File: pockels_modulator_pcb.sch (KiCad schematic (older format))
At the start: 11 parts, among them J1 Conn_Coaxial

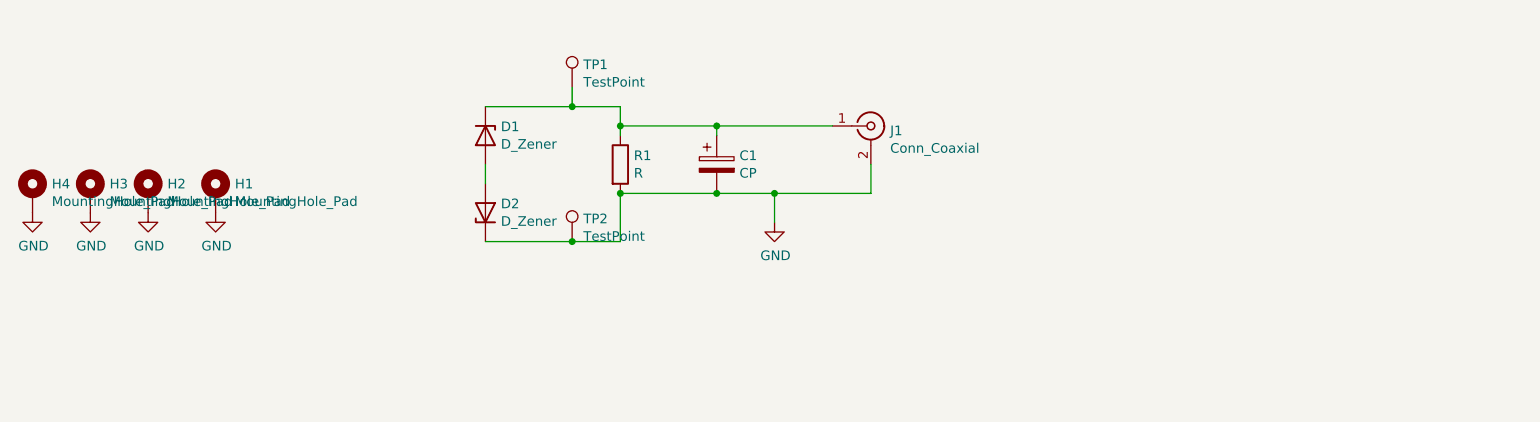
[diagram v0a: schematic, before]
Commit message: revised pockels modulator PCB to include thermal vias, chip for thermal sensing, SMD connector
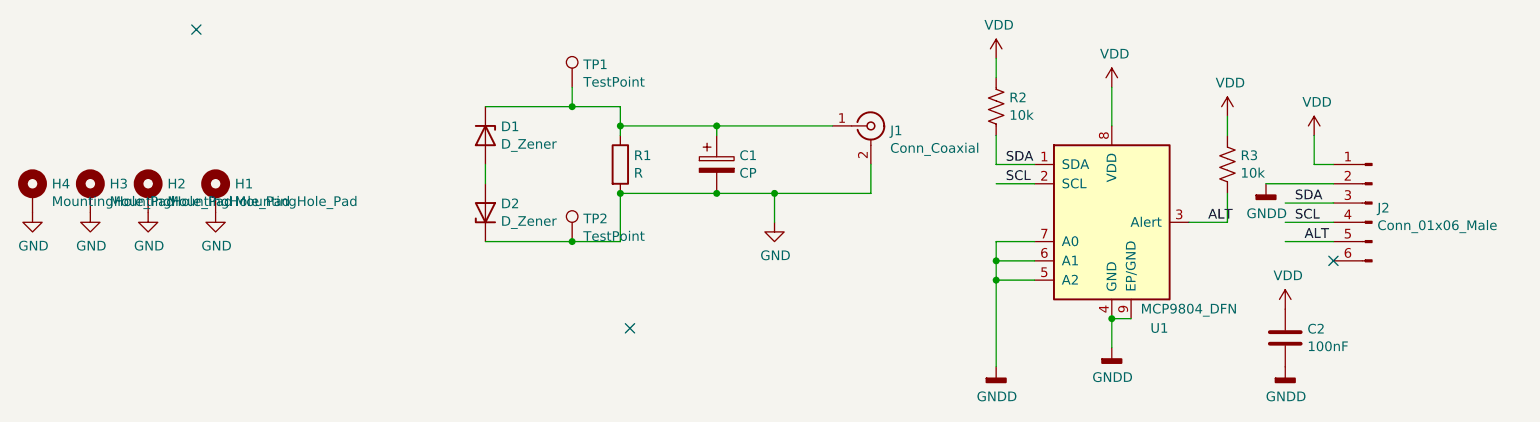
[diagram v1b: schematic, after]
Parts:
- added C2: 100nF, Capacitor_SMD:C_0805_2012Metric_Pad1.15x1.40mm_HandSolder, symbol Device:C
- added J2: Conn_01x06_Male, my_library_foot:S6B-XH-SM4-TB, symbol Connector:Conn_01x06_Male
- added R2, R3: 10k, Resistor_SMD:R_0805_2012Metric_Pad1.15x1.40mm_HandSolder, symbol Device:R_US
- added U1: MCP9804_DFN, Package_DFN_QFN:DFN-8-1EP_3x2mm_P0.5mm_EP1.3x1.5mm_HandSolder, symbol Sensor_Temperature:MCP9804_DFN
- C1: footprint my_library_foot:pockels_chip_10mm -> my_library_foot:pockels_chip_10mm_thermal
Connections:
- net labels added: ALT, GNDD, SCL, SDA, VDD
- wire segments 17 -> 39
- no-connect marks 0 -> 3
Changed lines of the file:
@@
 F 0 "C1" H 4968 3246 50  0000 L CNN
 F 1 "CP" H 4968 3155 50  0000 L CNN
-F 2 "my_library_foot:pockels_chip_10mm" H 4888 3050 50  0001 C CNN
+F 2 "my_library_foot:pockels_chip_10mm_thermal" H 4888 3050 50  0001 C CNN
 F 3 "~" H 4850 3200 50  0001 C CNN
 	1    4850 3200
@@
 	1    0    0    -1
 $EndComp
+$Comp
+L Sensor_Temperature:MCP9804_DFN U1
+U 1 1 5FF4B793
+P 6900 3500
+F 0 "U1" H 7100 2950 50  0000 L CNN
+F 1 "MCP9804_DFN" H 7050 3050 50  0000 L CNN
+F 2 "Package_DFN_QFN:DFN-8-1EP_3x2mm_P0.5mm_EP1.3x1.5mm_HandSolder" H 5800 3000 50  0001 C CNN
+F 3 "http://ww1.microchip.com/downloads/en/DeviceDoc/22203b.pdf" H 6650 3950 50  0001 C CNN
+	1    6900 3500
+	1    0    0    -1
+$EndComp
+$Comp
+L power:VDD #PWR04
+U 1 1 5FF4CD79
+P 6900 2800
+F 0 "#PWR04" H 6900 2650 50  0001 C CNN
+F 1 "VDD" H 6915 2973 50  0000 C CNN
+F 2 "" H 6900 2800 50  0001 C CNN
+F 3 "" H 6900 2800 50  0001 C CNN
+	1    6900 2800
+	1    0    0    -1
+$EndComp
+Wire Wire Line
+	6900 2800 6900 3000
+Wire Wire Line
+	8050 3200 7950 3200
+Wire Wire Line
+	7950 3200 7950 3050
+$Comp
+L power:VDD #PWR010
+U 1 1 5FF4FF71
+P 7950 3050
+F 0 "#PWR010" H 7950 2900 50  0001 C CNN
+F 1 "VDD" H 7965 3223 50  0000 C CNN
+F 2 "" H 7950 3050 50  0001 C CNN
+F 3 "" H 7950 3050 50  0001 C CNN
+	1    7950 3050
+	1    0    0    -1
+$EndComp
+Wire Wire Line
+	7700 3300 8050 3300
+Wire Wire Line
+	7800 3400 8050 3400
+Wire Wire Line
+	7800 3500 8050 3500
+Text Label 7850 3400 0    50   ~ 0
+SDA
+Text Label 7850 3500 0    50   ~ 0
+SCL
+Wire Wire Line
+	6500 3200 6300 3200
+Wire Wire Line
+	6500 3300 6300 3300
+Text Label 6350 3200 0    50   ~ 0
+SDA
+Text Label 6350 3300 0    50   ~ 0
+SCL
+Wire Wire Line
+	6500 3800 6300 3800
+Wire Wire Line
+	6500 3700 6300 3700
+Wire Wire Line
+	6300 3700 6300 3800
+Connection ~ 6300 3800
+Wire Wire Line
+	6500 3600 6300 3600
+Wire Wire Line
+	6300 3600 6300 3700
+Connection ~ 6300 3700
+Wire Wire Line
+	7000 4000 6900 4000
+Wire Wire Line
+	6900 4000 6900 4150
+Connection ~ 6900 4000
+Wire Wire Line
+	8050 3600 7800 3600
+Text Label 7900 3600 0    50   ~ 0
+ALT
+Wire Wire Line
+	7300 3500 7500 3500
+Text Label 7400 3500 0    50   ~ 0
+ALT
+$Comp
+L Device:C C2
+U 1 1 5FF59802
+P 7800 4100
+F 0 "C2" H 7915 4146 50  0000 L CNN
+F 1 "100nF" H 7915 4055 50  0000 L CNN
+F 2 "Capacitor_SMD:C_0805_2012Metric_Pad1.15x1.40mm_HandSolder" H 7838 3950 50  0001 C CNN
+F 3 "~" H 7800 4100 50  0001 C CNN
+	1    7800 4100
+	1    0    0    -1
+$EndComp
+$Comp
+L power:VDD #PWR08
+U 1 1 5FF5A155
+P 7800 3950
+F 0 "#PWR08" H 7800 3800 50  0001 C CNN
+F 1 "VDD" H 7815 4123 50  0000 C CNN
+F 2 "" H 7800 3950 50  0001 C CNN
+F 3 "" H 7800 3950 50  0001 C CNN
+	1    7800 3950
+	1    0    0    -1
+$EndComp
+$Comp
+L Device:R_US R3
+U 1 1 5FF5AD39
+P 7500 3200
+F 0 "R3" H 7568 3246 50  0000 L CNN
+F 1 "10k" H 7568 3155 50  0000 L CNN
+F 2 "Resistor_SMD:R_0805_2012Metric_Pad1.15x1.40mm_HandSolder" V 7540 3190 50  0001 C CNN
+F 3 "~" H 7500 3200 50  0001 C CNN
+	1    7500 3200
+	1    0    0    -1
+$EndComp
+Wire Wire Line
+	7500 3350 7500 3500
+$Comp
+L power:VDD #PWR06
+U 1 1 5FF5E3D3
+P 7500 2950
+F 0 "#PWR06" H 7500 2800 50  0001 C CNN
+F 1 "VDD" H 7515 3123 50  0000 C CNN
+F 2 "" H 7500 2950 50  0001 C CNN
+F 3 "" H 7500 2950 50  0001 C CNN
+	1    7500 2950
+	1    0    0    -1
+$EndComp
+Wire Wire Line
+	7500 2950 7500 3050
+$Comp
+L Device:R_US R2
+U 1 1 5FF5F423
+P 6300 2900
+F 0 "R2" H 6368 2946 50  0000 L CNN
+F 1 "10k" H 6368 2855 50  0000 L CNN
+F 2 "Resistor_SMD:R_0805_2012Metric_Pad1.15x1.40mm_HandSolder" V 6340 2890 50  0001 C CNN
+F 3 "~" H 6300 2900 50  0001 C CNN
+	1    6300 2900
+	1    0    0    -1
+$EndComp
+Wire Wire Line
+	6300 3050 6300 3200
+$Comp
+L power:VDD #PWR02
+U 1 1 5FF6033B
+P 6300 2650
+F 0 "#PWR02" H 6300 2500 50  0001 C CNN
+F 1 "VDD" H 6315 2823 50  0000 C CNN
+F 2 "" H 6300 2650 50  0001 C CNN
+F 3 "" H 6300 2650 50  0001 C CNN
+	1    6300 2650
+	1    0    0    -1
+$EndComp
+Wire Wire Line
+	6300 2650 6300 2750
+Wire Wire Line
+	6300 3800 6300 4250
+$Comp
+L power:GNDD #PWR0105
+U 1 1 5FF63E84
+P 6300 4250
+F 0 "#PWR0105" H 6300 4000 50  0001 C CNN
+F 1 "GNDD" H 6304 4095 50  0000 C CNN
+F 2 "" H 6300 4250 50  0001 C CNN
+F 3 "" H 6300 4250 50  0001 C CNN
+	1    6300 4250
+	1    0    0    -1
+$EndComp
+$Comp
+L power:GNDD #PWR0106
+U 1 1 5FF645C1
+P 6900 4150
+F 0 "#PWR0106" H 6900 3900 50  0001 C CNN
+F 1 "GNDD" H 6904 3995 50  0000 C CNN
+F 2 "" H 6900 4150 50  0001 C CNN
+F 3 "" H 6900 4150 50  0001 C CNN
+	1    6900 4150
+	1    0    0    -1
+$EndComp
+$Comp
+L power:GNDD #PWR0107
+U 1 1 5FF64A4E
+P 7800 4250
+F 0 "#PWR0107" H 7800 4000 50  0001 C CNN
+F 1 "GNDD" H 7804 4095 50  0000 C CNN
+F 2 "" H 7800 4250 50  0001 C CNN
+F 3 "" H 7800 4250 50  0001 C CNN
+	1    7800 4250
+	1    0    0    -1
+$EndComp
+$Comp
+L power:GNDD #PWR0108
+U 1 1 5FF65065
+P 7700 3300
+F 0 "#PWR0108" H 7700 3050 50  0001 C CNN
+F 1 "GNDD" H 7704 3145 50  0000 C CNN
+F 2 "" H 7700 3300 50  0001 C CNN
+F 3 "" H 7700 3300 50  0001 C CNN
+	1    7700 3300
+	1    0    0    -1
+$EndComp
+$Comp
+L Connector:Conn_01x06_Male J2
+U 1 1 5FF6D550
+P 8250 3400
+F 0 "J2" H 8222 3374 50  0000 R CNN
+F 1 "Conn_01x06_Male" H 8222 3283 50  0000 R CNN
+F 2 "my_library_foot:S6B-XH-SM4-TB" H 8250 3400 50  0001 C CNN
+F 3 "~" H 8250 3400 50  0001 C CNN
+	1    8250 3400
+	-1   0    0    -1
+$EndComp
+NoConn ~ 8050 3700
+NoConn ~ 4400 4050
+NoConn ~ 2150 2500
 $EndSCHEMATC

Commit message: updated for new 5mm chips to version 3
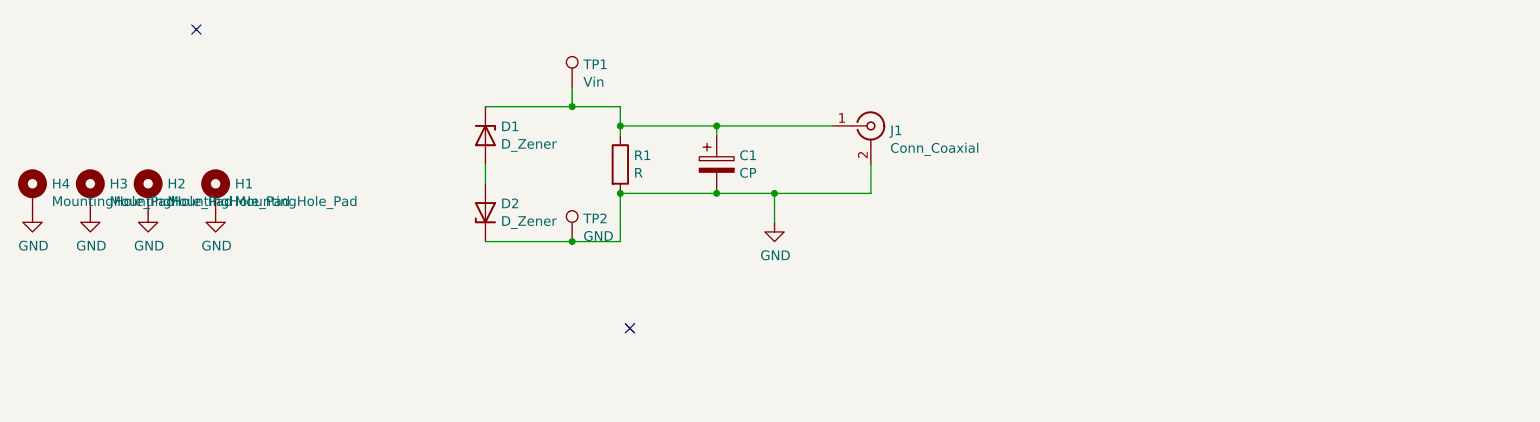
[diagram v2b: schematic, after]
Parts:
- removed C2: 100nF, Capacitor_SMD:C_0805_2012Metric_Pad1.15x1.40mm_HandSolder, symbol Device:C
- removed J2: Conn_01x06_Male, my_library_foot:S6B-XH-SM4-TB, symbol Connector:Conn_01x06_Male
- removed R2, R3: 10k, Resistor_SMD:R_0805_2012Metric_Pad1.15x1.40mm_HandSolder, symbol Device:R_US
- removed U1: MCP9804_DFN, Package_DFN_QFN:DFN-8-1EP_3x2mm_P0.5mm_EP1.3x1.5mm_HandSolder, symbol Sensor_Temperature:MCP9804_DFN
- TP1: value TestPoint -> Vin
- TP2: value TestPoint -> GND
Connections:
- net labels removed: ALT, GNDD, SCL, SDA, VDD
- wire segments 39 -> 17
- no-connect marks 3 -> 2
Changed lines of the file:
@@
 P 4100 2800
 F 0 "TP1" H 4158 2918 50  0000 L CNN
-F 1 "TestPoint" H 4158 2827 50  0000 L CNN
+F 1 "Vin" H 4158 2827 50  0000 L CNN
 F 2 "my_library_foot:TestPoint_Keystone_5000-5004_Miniature" H 4300 2800 50  0001 C CNN
 F 3 "~" H 4300 2800 50  0001 C CNN
@@
 P 4100 3600
 F 0 "TP2" H 4158 3718 50  0000 L CNN
-F 1 "TestPoint" H 4158 3627 50  0000 L CNN
+F 1 "GND" H 4158 3627 50  0000 L CNN
 F 2 "my_library_foot:TestPoint_Keystone_5000-5004_Miniature" H 4300 3600 50  0001 C CNN
 F 3 "~" H 4300 3600 50  0001 C CNN
@@
 	1    0    0    -1
 $EndComp
-$Comp
-L Sensor_Temperature:MCP9804_DFN U1
-U 1 1 5FF4B793
-P 6900 3500
-F 0 "U1" H 7100 2950 50  0000 L CNN
-F 1 "MCP9804_DFN" H 7050 3050 50  0000 L CNN
-F 2 "Package_DFN_QFN:DFN-8-1EP_3x2mm_P0.5mm_EP1.3x1.5mm_HandSolder" H 5800 3000 50  0001 C CNN
-F 3 "http://ww1.microchip.com/downloads/en/DeviceDoc/22203b.pdf" H 6650 3950 50  0001 C CNN
-	1    6900 3500
-	1    0    0    -1
-$EndComp
-$Comp
-L power:VDD #PWR04
-U 1 1 5FF4CD79
-P 6900 2800
-F 0 "#PWR04" H 6900 2650 50  0001 C CNN
-F 1 "VDD" H 6915 2973 50  0000 C CNN
-F 2 "" H 6900 2800 50  0001 C CNN
-F 3 "" H 6900 2800 50  0001 C CNN
-	1    6900 2800
-	1    0    0    -1
-$EndComp
-Wire Wire Line
-	6900 2800 6900 3000
-Wire Wire Line
-	8050 3200 7950 3200
-Wire Wire Line
-	7950 3200 7950 3050
-$Comp
-L power:VDD #PWR010
-U 1 1 5FF4FF71
-P 7950 3050
-F 0 "#PWR010" H 7950 2900 50  0001 C CNN
-F 1 "VDD" H 7965 3223 50  0000 C CNN
-F 2 "" H 7950 3050 50  0001 C CNN
-F 3 "" H 7950 3050 50  0001 C CNN
-	1    7950 3050
-	1    0    0    -1
-$EndComp
-Wire Wire Line
-	7700 3300 8050 3300
-Wire Wire Line
-	7800 3400 8050 3400
-Wire Wire Line
-	7800 3500 8050 3500
-Text Label 7850 3400 0    50   ~ 0
-SDA
-Text Label 7850 3500 0    50   ~ 0
-SCL
-Wire Wire Line
-	6500 3200 6300 3200
-Wire Wire Line
-	6500 3300 6300 3300
-Text Label 6350 3200 0    50   ~ 0
-SDA
-Text Label 6350 3300 0    50   ~ 0
-SCL
-Wire Wire Line
-	6500 3800 6300 3800
-Wire Wire Line
-	6500 3700 6300 3700
-Wire Wire Line
-	6300 3700 6300 3800
-Connection ~ 6300 3800
-Wire Wire Line
-	6500 3600 6300 3600
-Wire Wire Line
-	6300 3600 6300 3700
-Connection ~ 6300 3700
-Wire Wire Line
-	7000 4000 6900 4000
-Wire Wire Line
-	6900 4000 6900 4150
-Connection ~ 6900 4000
-Wire Wire Line
-	8050 3600 7800 3600
-Text Label 7900 3600 0    50   ~ 0
-ALT
-Wire Wire Line
-	7300 3500 7500 3500
-Text Label 7400 3500 0    50   ~ 0
-ALT
-$Comp
-L Device:C C2
-U 1 1 5FF59802
-P 7800 4100
-F 0 "C2" H 7915 4146 50  0000 L CNN
-F 1 "100nF" H 7915 4055 50  0000 L CNN
-F 2 "Capacitor_SMD:C_0805_2012Metric_Pad1.15x1.40mm_HandSolder" H 7838 3950 50  0001 C CNN
-F 3 "~" H 7800 4100 50  0001 C CNN
-	1    7800 4100
-	1    0    0    -1
-$EndComp
-$Comp
-L power:VDD #PWR08
-U 1 1 5FF5A155
-P 7800 3950
-F 0 "#PWR08" H 7800 3800 50  0001 C CNN
-F 1 "VDD" H 7815 4123 50  0000 C CNN
-F 2 "" H 7800 3950 50  0001 C CNN
-F 3 "" H 7800 3950 50  0001 C CNN
-	1    7800 3950
-	1    0    0    -1
-$EndComp
-$Comp
-L Device:R_US R3
-U 1 1 5FF5AD39
-P 7500 3200
-F 0 "R3" H 7568 3246 50  0000 L CNN
-F 1 "10k" H 7568 3155 50  0000 L CNN
-F 2 "Resistor_SMD:R_0805_2012Metric_Pad1.15x1.40mm_HandSolder" V 7540 3190 50  0001 C CNN
-F 3 "~" H 7500 3200 50  0001 C CNN
-	1    7500 3200
-	1    0    0    -1
-$EndComp
-Wire Wire Line
-	7500 3350 7500 3500
-$Comp
-L power:VDD #PWR06
-U 1 1 5FF5E3D3
-P 7500 2950
-F 0 "#PWR06" H 7500 2800 50  0001 C CNN
-F 1 "VDD" H 7515 3123 50  0000 C CNN
-F 2 "" H 7500 2950 50  0001 C CNN
-F 3 "" H 7500 2950 50  0001 C CNN
-	1    7500 2950
-	1    0    0    -1
-$EndComp
-Wire Wire Line
-	7500 2950 7500 3050
-$Comp
-L Device:R_US R2
-U 1 1 5FF5F423
-P 6300 2900
-F 0 "R2" H 6368 2946 50  0000 L CNN
-F 1 "10k" H 6368 2855 50  0000 L CNN
-F 2 "Resistor_SMD:R_0805_2012Metric_Pad1.15x1.40mm_HandSolder" V 6340 2890 50  0001 C CNN
-F 3 "~" H 6300 2900 50  0001 C CNN
-	1    6300 2900
-	1    0    0    -1
-$EndComp
-Wire Wire Line
-	6300 3050 6300 3200
-$Comp
-L power:VDD #PWR02
-U 1 1 5FF6033B
-P 6300 2650
-F 0 "#PWR02" H 6300 2500 50  0001 C CNN
-F 1 "VDD" H 6315 2823 50  0000 C CNN
-F 2 "" H 6300 2650 50  0001 C CNN
-F 3 "" H 6300 2650 50  0001 C CNN
-	1    6300 2650
-	1    0    0    -1
-$EndComp
-Wire Wire Line
-	6300 2650 6300 2750
-Wire Wire Line
-	6300 3800 6300 4250
-$Comp
-L power:GNDD #PWR0105
-U 1 1 5FF63E84
-P 6300 4250
-F 0 "#PWR0105" H 6300 4000 50  0001 C CNN
-F 1 "GNDD" H 6304 4095 50  0000 C CNN
-F 2 "" H 6300 4250 50  0001 C CNN
-F 3 "" H 6300 4250 50  0001 C CNN
-	1    6300 4250
-	1    0    0    -1
-$EndComp
-$Comp
-L power:GNDD #PWR0106
-U 1 1 5FF645C1
-P 6900 4150
-F 0 "#PWR0106" H 6900 3900 50  0001 C CNN
-F 1 "GNDD" H 6904 3995 50  0000 C CNN
-F 2 "" H 6900 4150 50  0001 C CNN
-F 3 "" H 6900 4150 50  0001 C CNN
-	1    6900 4150
-	1    0    0    -1
-$EndComp
-$Comp
-L power:GNDD #PWR0107
-U 1 1 5FF64A4E
-P 7800 4250
-F 0 "#PWR0107" H 7800 4000 50  0001 C CNN
-F 1 "GNDD" H 7804 4095 50  0000 C CNN
-F 2 "" H 7800 4250 50  0001 C CNN
-F 3 "" H 7800 4250 50  0001 C CNN
-	1    7800 4250
-	1    0    0    -1
-$EndComp
-$Comp
-L power:GNDD #PWR0108
-U 1 1 5FF65065
-P 7700 3300
-F 0 "#PWR0108" H 7700 3050 50  0001 C CNN
-F 1 "GNDD" H 7704 3145 50  0000 C CNN
-F 2 "" H 7700 3300 50  0001 C CNN
-F 3 "" H 7700 3300 50  0001 C CNN
-	1    7700 3300
-	1    0    0    -1
-$EndComp
-$Comp
-L Connector:Conn_01x06_Male J2
-U 1 1 5FF6D550
-P 8250 3400
-F 0 "J2" H 8222 3374 50  0000 R CNN
-F 1 "Conn_01x06_Male" H 8222 3283 50  0000 R CNN
-F 2 "my_library_foot:S6B-XH-SM4-TB" H 8250 3400 50  0001 C CNN
-F 3 "~" H 8250 3400 50  0001 C CNN
-	1    8250 3400
-	-1   0    0    -1
-$EndComp
-NoConn ~ 8050 3700
 NoConn ~ 4400 4050
 NoConn ~ 2150 2500
